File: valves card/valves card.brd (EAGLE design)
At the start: 100 x 80 mm, 68 parts, among them J1 TBP02R1-381-14BE, J2 09231486921, M1 SAM_D21_MINI_BREAKOUT, T1 IRLZ44NSTRLPBF, T10 IRLZ44NSTRLPBF, T11 IRLZ44NSTRLPBF, T12 IRLZ44NSTRLPBF, T2 IRLZ44NSTRLPBF, T3 IRLZ44NSTRLPBF, T4 IRLZ44NSTRLPBF, T5 IRLZ44NSTRLPBF, T6 IRLZ44NSTRLPBF, T7 IRLZ44NSTRLPBF, T8 IRLZ44NSTRLPBF, T9 IRLZ44NSTRLPBF, U1 LM2937IMP-12, U10 EL817(D)-ND, U11 EL817(D)-ND, U12 EL817(D)-ND, U13 EL817(D)-ND, U2 EL817(D)-ND, U3 EL817(D)-ND, U4 EL817(D)-ND, U5 EL817(D)-ND, U6 EL817(D)-ND, U7 EL817(D)-ND, U8 EL817(D)-ND, U9 EL817(D)-ND

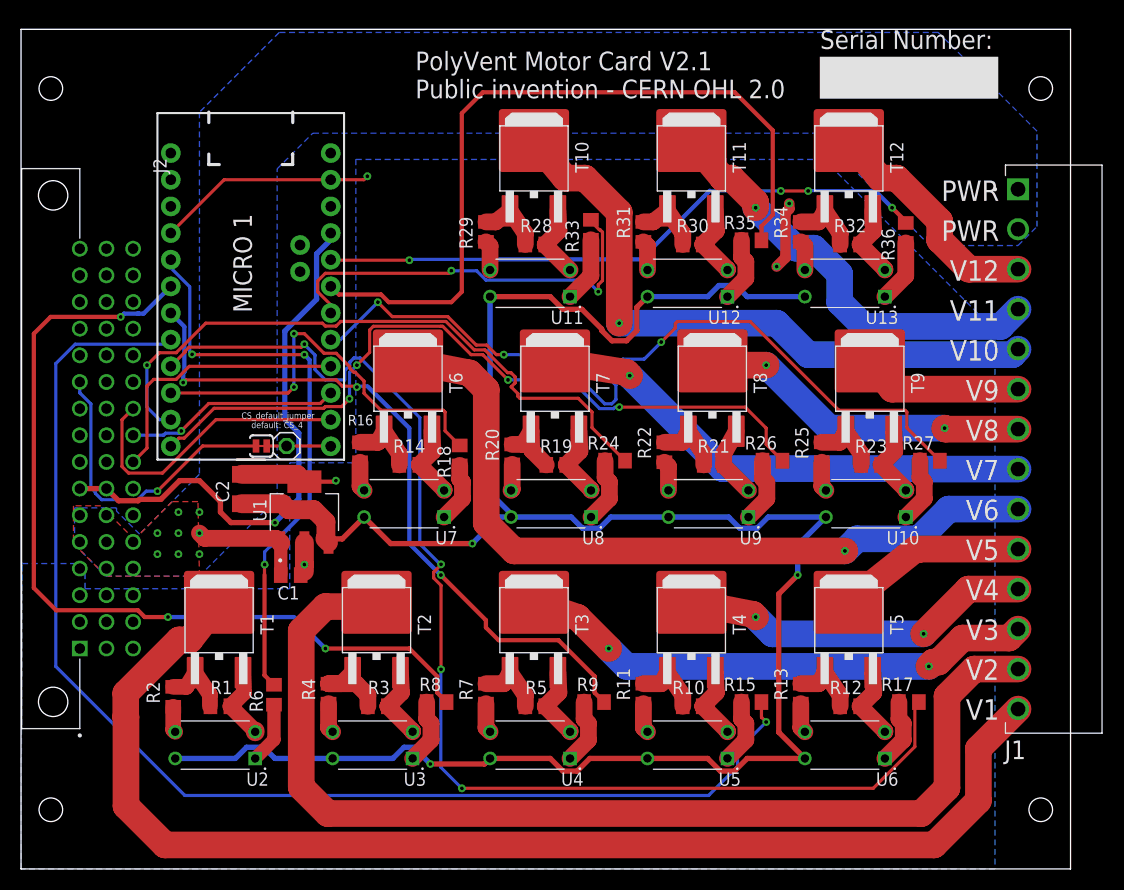
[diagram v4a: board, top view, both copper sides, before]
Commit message: made card holes bigger, started usb port work, but I'm not done that part yet
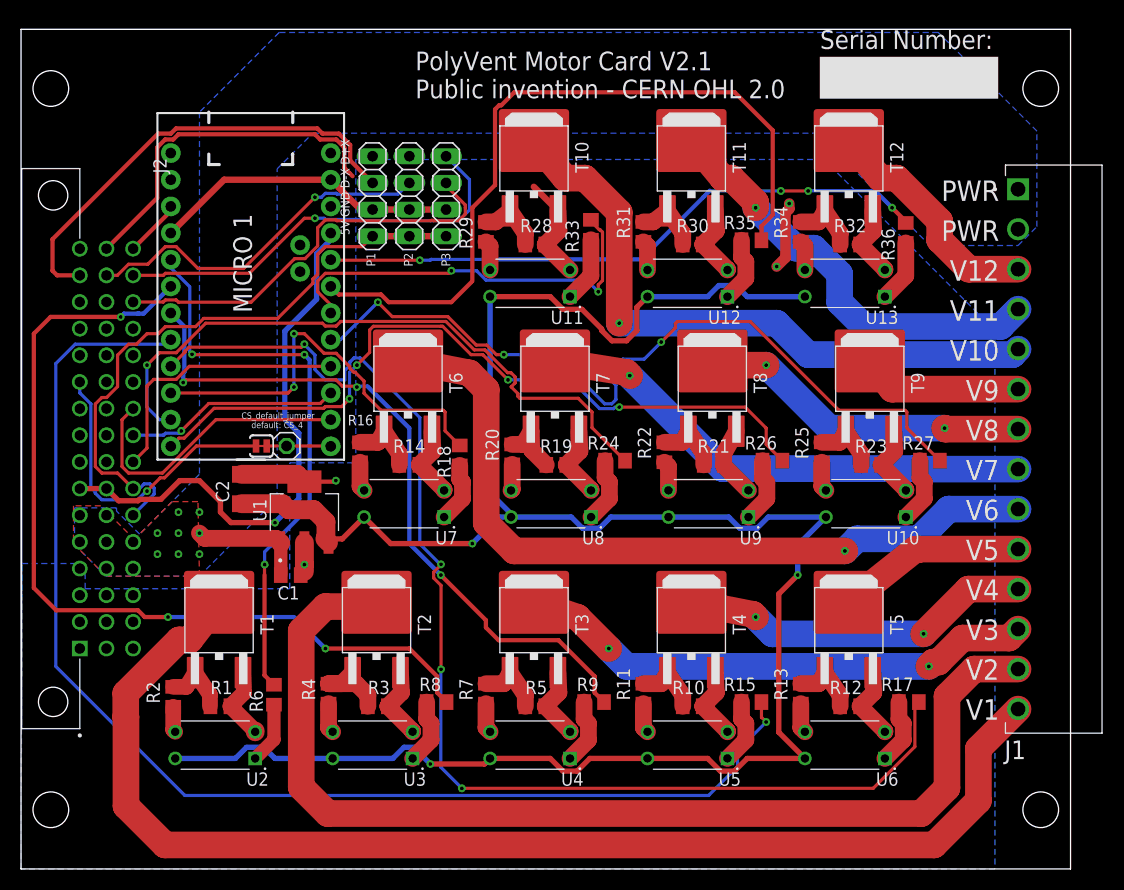
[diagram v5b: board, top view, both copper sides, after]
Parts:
- added JP2, JP3, JP4: (no value), pinhead:1X04
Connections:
- net 5V: now also JP2.1, JP3.1, JP4.1
- net GND: now also JP2.2, JP3.2, JP4.2
- net USB1_D+: now also JP2.4
- net USB1_D-: now also JP2.3
- net USB2_D+: now also JP3.4
- net USB2_D-: now also JP3.3
- net USB3_D+: now also JP4.4
- net USB3_D-: now also JP4.3
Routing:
- net 5V: track 0.00 -> 59.3 mm
- net USB1_D-: track 0.00 -> 43.7 mm
- net USB3_D+: track 0.00 -> 40.9 mm, vias 0 -> 1
- net USB3_D-: track 0.00 -> 40.1 mm
- net USB2_D-: track 0.00 -> 34.3 mm, vias 0 -> 1
- net USB2_D+: track 0.00 -> 33.6 mm
- net GND: track 125.7 -> 137.4 mm, vias 5 -> 4
- net RESET: track 0.00 -> 5.52 mm
- net SOL11: track 73.4 -> 71.8 mm
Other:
- board text added: "5V GND D-X D+X"
- board text added: "P1 P2 P3"

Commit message: USB system mods complete on the main board, valves board, and motor board
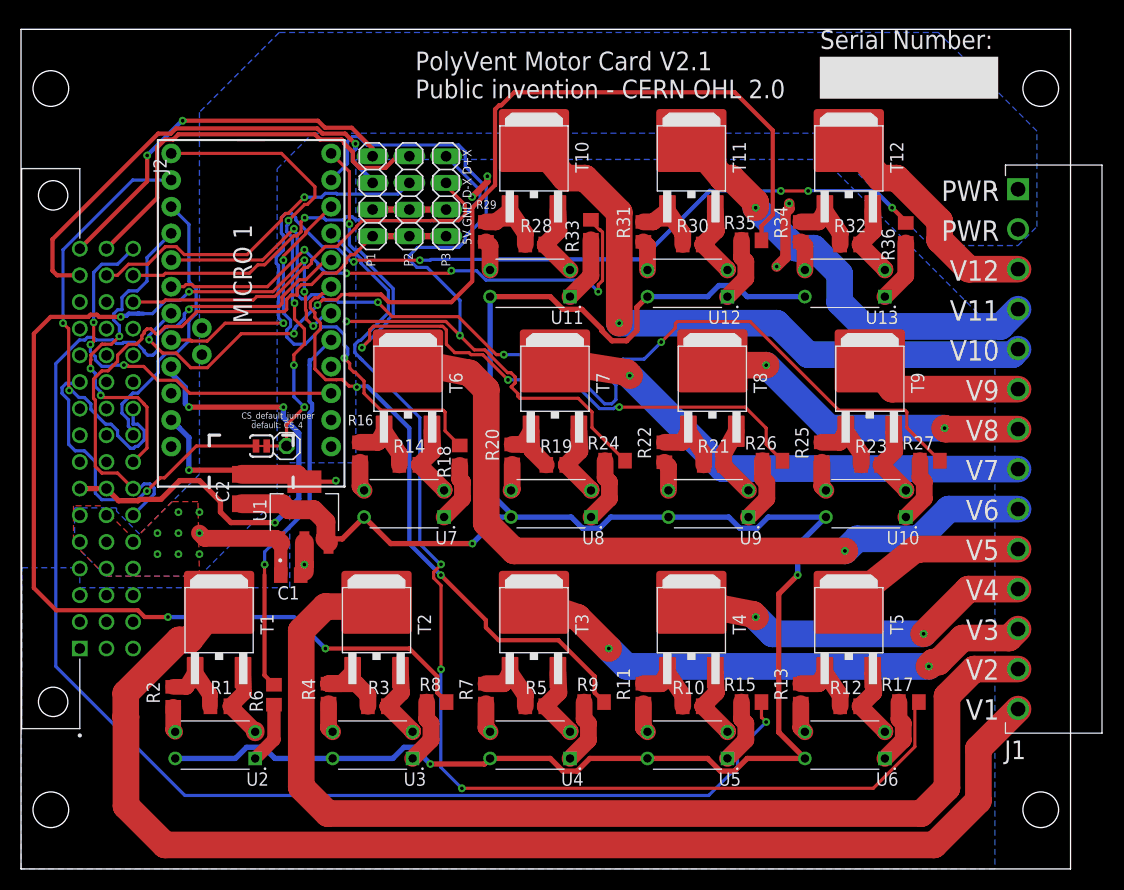
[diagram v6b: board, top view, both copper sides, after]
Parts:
- removed M1: SAM_D21_MINI_BREAKOUT, SparkFun-SAMD21-Mini-Breakout:JP1_SPARKFUN-SAMD21-MINI-BREAKOUT-V10
- added M2: SAM_D21_MINI_BREAKOUT, SparkFun-SAMD21-Mini-Breakout:JP1_SPARKFUN-SAMD21-MINI-BREAKOUT-V10
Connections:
- new net N$1: M2.9@JP1
- net 3.3V: now also M2.4@JP2; no longer M1.4@JP2
- net AREF: now also M2.3@JP2; no longer M1.3@JP2
- net GND: now also M2.2@JP2; no longer M1.2@JP2, M1.9@JP1
- net MISO: now also M2.10@JP2; no longer M1.10@JP2
- net MOSI: now also M2.11@JP2; no longer M1.11@JP2
- net N$2: now also M2.12@JP2; no longer M1.12@JP2
- net RESET: now also M2.10@JP1; no longer M1.10@JP1
- net SCK: now also M2.9@JP2; no longer M1.9@JP2
- net SOL1: now also M2.8@JP1; no longer M1.8@JP1
- net SOL10: now also M2.7@JP2; no longer M1.7@JP2
- net SOL11: now also M2.6@JP2; no longer M1.6@JP2
- net SOL12: now also M2.5@JP2; no longer M1.5@JP2
- net SOL2: now also M2.7@JP1; no longer M1.7@JP1
- net SOL3: now also M2.6@JP1; no longer M1.6@JP1
- net SOL4: now also M2.5@JP1; no longer M1.5@JP1
- net SOL5: now also M2.4@JP1; no longer M1.4@JP1
- net SOL6: now also M2.3@JP1; no longer M1.3@JP1
- net SOL7: now also M2.2@JP1; no longer M1.2@JP1
- net SOL8: now also M2.1@JP1; no longer M1.1@JP1
- net SOL9: now also M2.8@JP2; no longer M1.8@JP2
- net VIN: now also M2.1@JP2; no longer M1.1@JP2
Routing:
- net N$2: track 6.11 -> 45.1 mm, vias 0 -> 4
- net USB1_D+: track 0.00 -> 36.2 mm, vias 0 -> 2
- net RESET: track 5.52 -> 37.2 mm, vias 0 -> 3
- net SOL12: track 59.8 -> 88.9 mm, vias 4 -> 6
- net SOL11: track 71.8 -> 96.4 mm, vias 0 -> 3
- net SOL2: track 84.0 -> 106.7 mm, vias 3 -> 7
- net SOL9: track 75.5 -> 97.2 mm, vias 3 -> 4
- net SOL4: track 119.4 -> 141.0 mm, vias 1 -> 2
- net SOL1: track 54.4 -> 36.6 mm, vias 3 -> 1
- net SOL7: track 61.9 -> 76.8 mm, vias 1 -> 2
- net SOL10: track 39.7 -> 52.5 mm, vias 2 -> 4
- net MOSI: track 28.2 -> 40.7 mm, vias 0 -> 2
- net GND: track 137.4 -> 126.1 mm, vias 4 -> 7
- net SOL3: track 68.1 -> 58.2 mm, vias 3 -> 2
- net SOL5: track 117.7 -> 110.9 mm, vias 4 -> 3
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
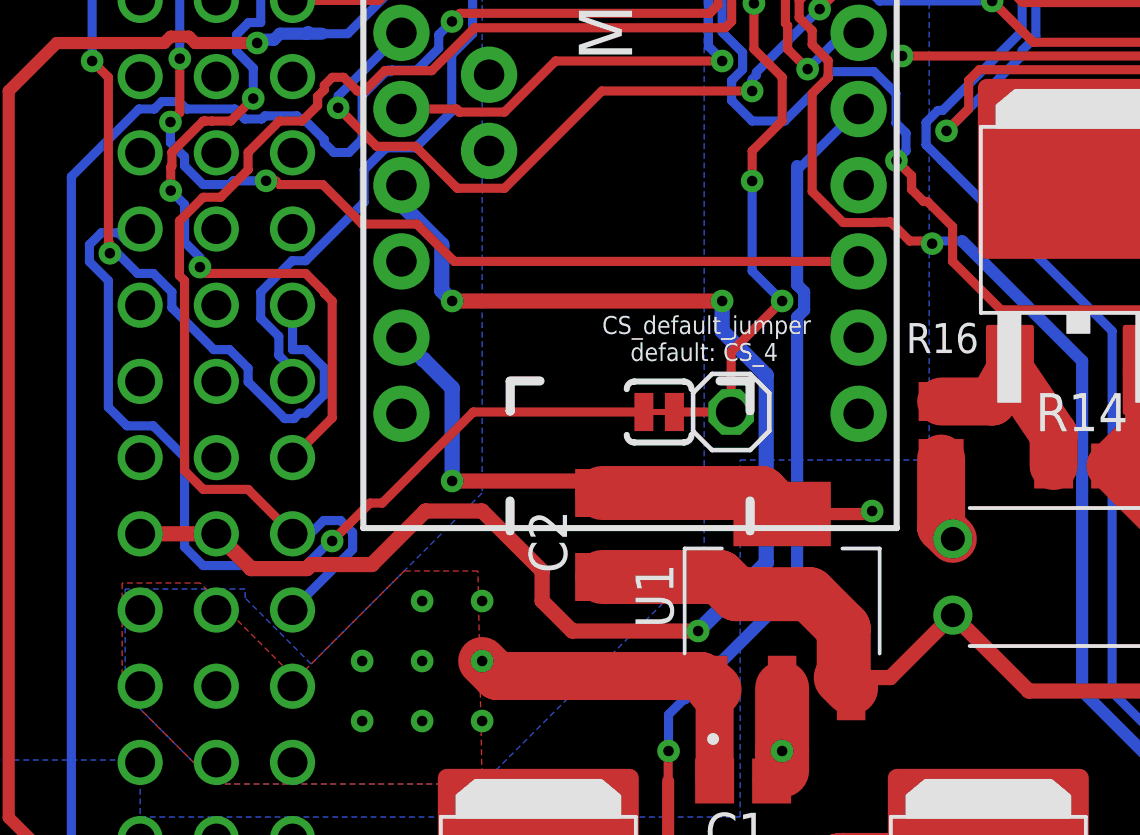
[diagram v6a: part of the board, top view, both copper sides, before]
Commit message: added on light to main card
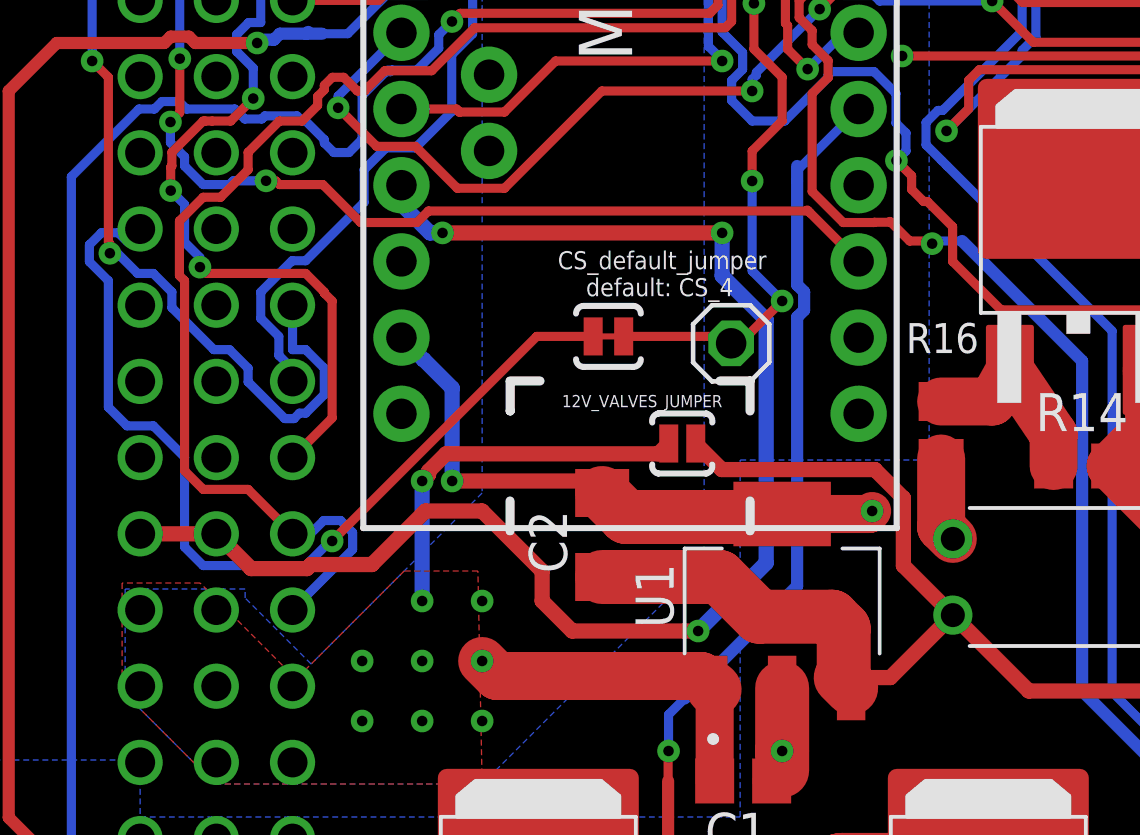
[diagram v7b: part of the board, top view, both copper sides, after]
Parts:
- added 12V_VALVES_JUMPER: (no value), SparkFun-Passives:SJ_2S-NO
- moved SJ1 3.03 mm to (21.2, 42.8)
- moved JP1 2.29 mm to (25.3, 42.6)
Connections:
- net 12V: now also 12V_VALVES_JUMPER.2
- net 24V/12V: now also 12V_VALVES_JUMPER.1
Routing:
- net 24V/12V: track 11.3 -> 24.1 mm, vias 8 -> 9
- net 12V: track 211.6 -> 223.8 mm
- net CS_4: track 31.7 -> 31.1 mm

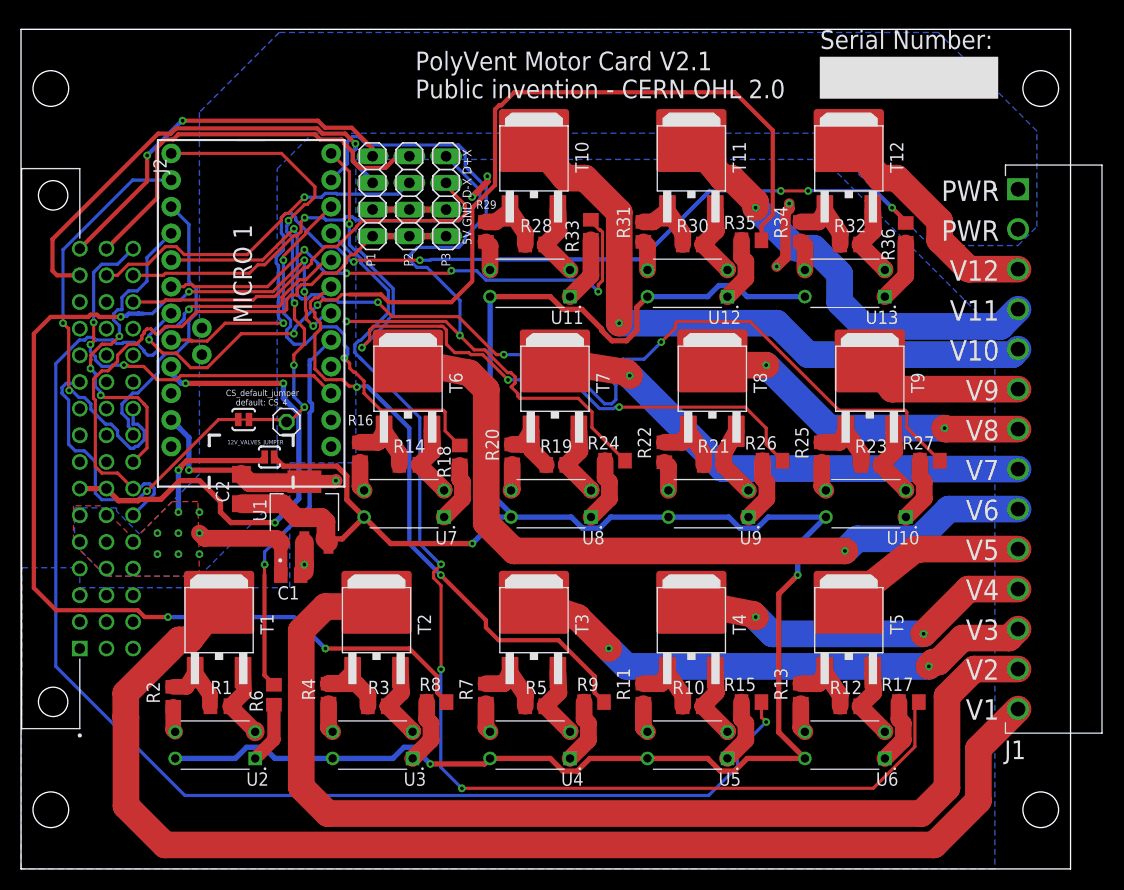
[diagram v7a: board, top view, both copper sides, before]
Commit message: final mods to the boards, next commit will add the CAM data, it will be the final commit before the polyvent V2.1 design merge, and I'm ready to order boards
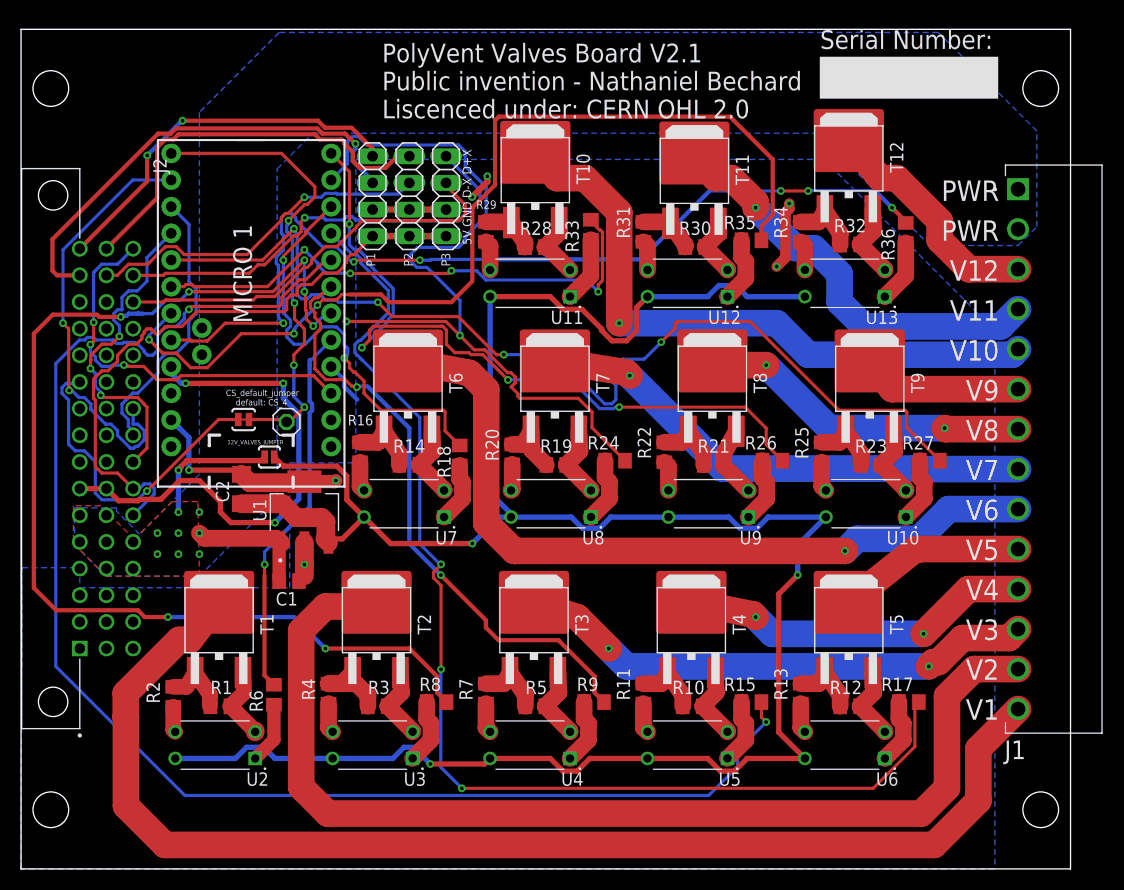
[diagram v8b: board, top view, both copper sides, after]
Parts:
- moved T11 1.22 mm to (64.3, 63.8)
- moved T10 1.13 mm to (49.1, 63.9)
- moved C1 0.59 mm to (25.5, 27.4)
- moved R30 0.34 mm to (64.2, 59.3)
- moved R28 0.25 mm to (49.0, 59.2)
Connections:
- removed net N$1: M2.9@JP1
- net GND: now also M2.9@JP1
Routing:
- net SOL11: track 96.4 -> 92.2 mm
- net GND: track 126.2 -> 128.7 mm
- net N$63: track 6.30 -> 5.18 mm
- net N$69: track 6.30 -> 5.32 mm
- net DRAIN11: track 41.2 -> 40.4 mm
- net 24V/12V: track 24.1 -> 24.8 mm
- net DRAIN10: track 61.2 -> 60.5 mm
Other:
- board text added: "PolyVent Valves Board V2.1 Public invention - Nathaniel Bechard Liscenced under: CERN OHL 2.0"
- board text removed: "PolyVent Motor Card V2.1 Public invention - CERN OHL 2.0"
